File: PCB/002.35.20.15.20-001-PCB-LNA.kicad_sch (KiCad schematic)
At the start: 10 parts, among them J1 Conn_Coaxial, J2 Conn_Coaxial, J3 Conn_Coaxial, U3 YAT-1A+, U4 L7805, U5 L7805

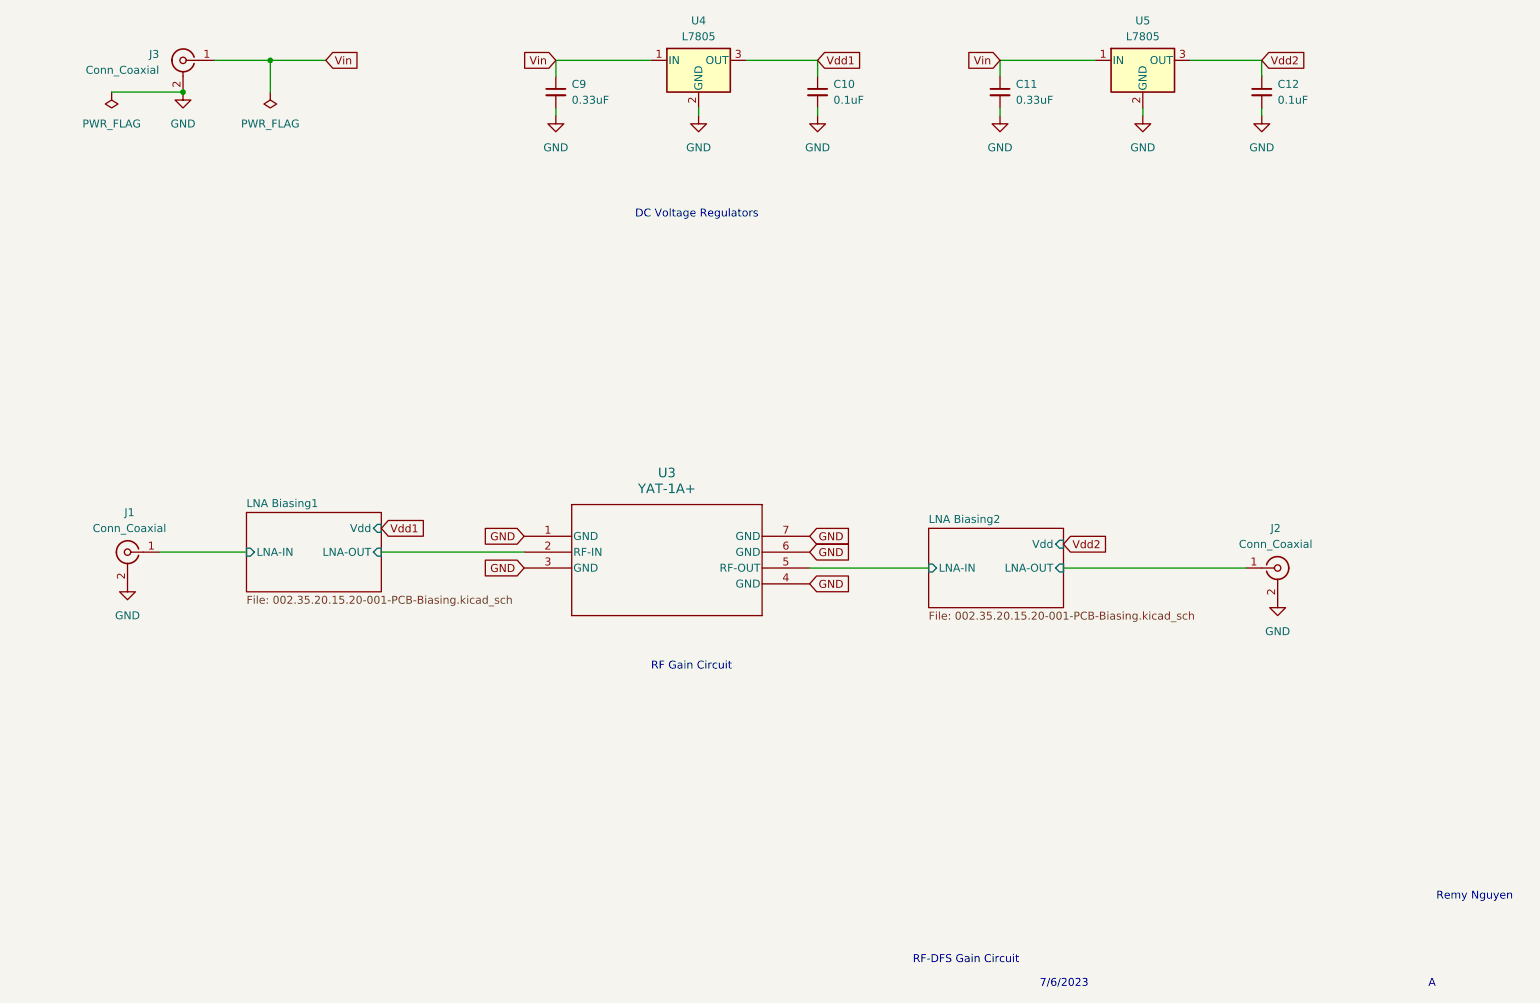
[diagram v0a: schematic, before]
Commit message: PCB Rev B complete: compacted board and fixed sma pads
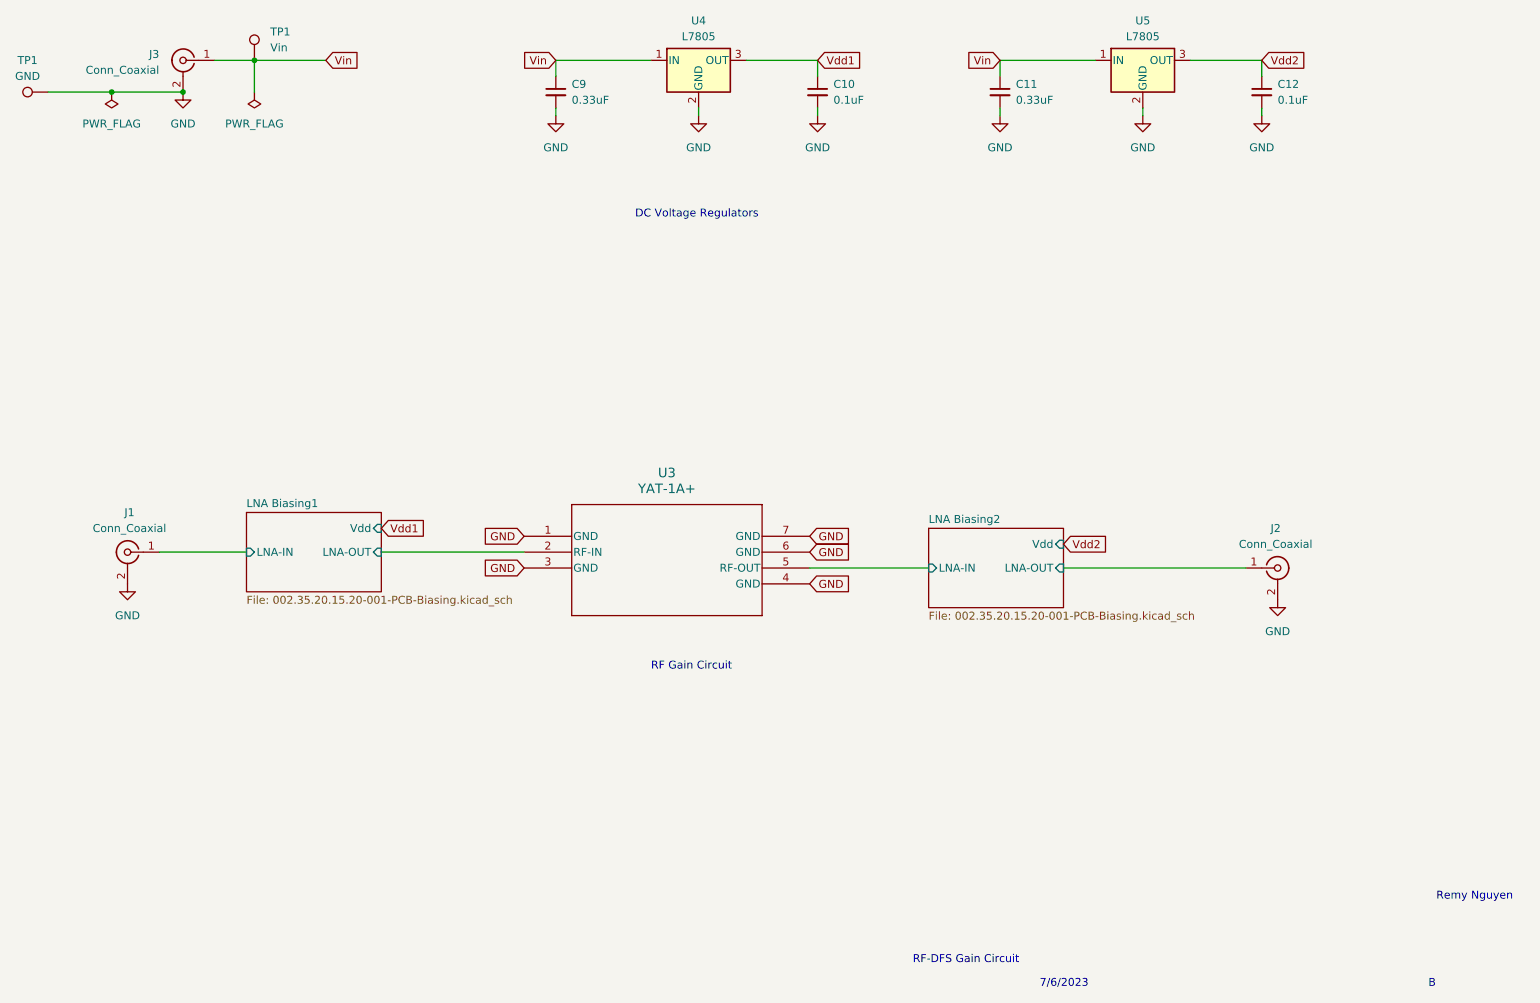
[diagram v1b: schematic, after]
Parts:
- added TP1: GND, TestPoint:TestPoint_Loop_D2.54mm_Drill1.5mm_Beaded, symbol Connector:TestPoint
- added TP1: Vin, TestPoint:TestPoint_Loop_D2.54mm_Drill1.5mm_Beaded, symbol Connector:TestPoint
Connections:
- net GND: now also TP1.1
- net Vin: now also TP1.1
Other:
- note added: "B"
- note removed: "A"
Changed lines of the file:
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@@
   (junction (at 69.85 50.8) (diameter 0) (color 0 0 0 0)
   )
-  (junction (at 83.82 45.72) (diameter 0) (color 0 0 0 0)
+  (junction (at 58.42 50.8) (diameter 0) (color 0 0 0 0)
+  )
+  (junction (at 81.28 45.72) (diameter 0) (color 0 0 0 0)
   )
   (wire (pts (xy 223.52 53.34) (xy 223.52 54.61))
@@
     (stroke (width 0) (type default))
   )
-  (wire (pts (xy 92.71 45.72) (xy 83.82 45.72))
-    (stroke (width 0) (type default))
-  )
   (wire (pts (xy 66.04 124.46) (xy 80.01 124.46))
     (stroke (width 0) (type default))
   )
-  (wire (pts (xy 83.82 45.72) (xy 74.93 45.72))
-    (stroke (width 0) (type default))
-  )
   (wire (pts (xy 129.54 48.26) (xy 129.54 45.72))
     (stroke (width 0) (type default))
@@
     (stroke (width 0) (type default))
   )
+  (wire (pts (xy 48.26 50.8) (xy 58.42 50.8))
+    (stroke (width 0) (type default))
+  )
   (wire (pts (xy 200.66 45.72) (xy 215.9 45.72))
     (stroke (width 0) (type default))
   )
+  (wire (pts (xy 81.28 45.72) (xy 92.71 45.72))
+    (stroke (width 0) (type default))
+  )
   (wire (pts (xy 210.82 127) (xy 240.03 127))
     (stroke (width 0) (type default))
   )
-  (wire (pts (xy 83.82 45.72) (xy 83.82 50.8))
+  (wire (pts (xy 81.28 45.72) (xy 81.28 50.8))
     (stroke (width 0) (type default))
   )
@@
   )
   (wire (pts (xy 242.57 53.34) (xy 242.57 54.61))
+    (stroke (width 0) (type default))
+  )
+  (wire (pts (xy 74.93 45.72) (xy 81.28 45.72))
     (stroke (width 0) (type default))
   )
@@
     (effects (font (size 1.27 1.27)) (justify left bottom))
   )
-  (text "A" (at 269.24 194.31 0)
+  (text "B" (at 269.24 194.31 0)
     (effects (font (size 1.27 1.27)) (justify left bottom))
   )
@@
     )
   )
+  (symbol (lib_id "Connector:TestPoint") (at 48.26 50.8 90) (unit 1)
+    (in_bom yes) (on_board yes) (dnp no) (fields_autoplaced)
+    (property "Reference" "TP1" (at 44.958 45.72 90)
+      (effects (font (size 1.27 1.27)))
+    )
+    (property "Value" "GND" (at 44.958 48.26 90)
+      (effects (font (size 1.27 1.27)))
+    )
+    (property "Footprint" "TestPoint:TestPoint_Loop_D2.54mm_Drill1.5mm_Beaded" (at 48.26 45.72 0)
+      (effects (font (size 1.27 1.27)) hide)
+    )
+    (property "Datasheet" "~" (at 48.26 45.72 0)
+      (effects (font (size 1.27 1.27)) hide)
+    )
+    (pin "1")
+    (instances
+      (project "002.35.20.15.20-001-PCB-LNA"
+        (path "/a33db424-96f2-4015-ba95-8b9f2330ef17/9ff85c99-1040-4eb9-b5d8-3cc01caa0e77"
+          (reference "TP1") (unit 1)
+        )
+        (path "/a33db424-96f2-4015-ba95-8b9f2330ef17/ba672304-1315-4178-9e1d-d553703e5b04"
+          (reference "TP2") (unit 1)
+        )
+        (path "/a33db424-96f2-4015-ba95-8b9f2330ef17"
+          (reference "TP4") (unit 1)
+        )
+      )
+    )
+  )
   (symbol (lib_id "power:GND") (at 152.4 54.61 0) (unit 1)
     (in_bom yes) (on_board yes) (dnp no) (fields_autoplaced)
@@
     )
   )
-  (symbol (lib_id "power:PWR_FLAG") (at 83.82 50.8 180) (unit 1)
-    (in_bom yes) (on_board yes) (dnp no) (fields_autoplaced)
-    (property "Reference" "#FLG01" (at 83.82 52.705 0)
-      (effects (font (size 1.27 1.27)) hide)
-    )
-    (property "Value" "PWR_FLAG" (at 83.82 55.88 0)
-      (effects (font (size 1.27 1.27)))
-    )
-    (property "Footprint" "" (at 83.82 50.8 0)
-      (effects (font (size 1.27 1.27)) hide)
-    )
-    (property "Datasheet" "~" (at 83.82 50.8 0)
-      (effects (font (size 1.27 1.27)) hide)
-    )
+  (symbol (lib_id "Connector:TestPoint") (at 81.28 45.72 0) (unit 1)
+    (in_bom yes) (on_board yes) (dnp no) (fields_autoplaced)
+    (property "Reference" "TP1" (at 83.82 41.148 0)
+      (effects (font (size 1.27 1.27)) (justify left))
+    )
+    (property "Value" "Vin" (at 83.82 43.688 0)
+      (effects (font (size 1.27 1.27)) (justify left))
+    )
+    (property "Footprint" "TestPoint:TestPoint_Loop_D2.54mm_Drill1.5mm_Beaded" (at 86.36 45.72 0)
+      (effects (font (size 1.27 1.27)) hide)
+    )
+    (property "Datasheet" "~" (at 86.36 45.72 0)
+      (effects (font (size 1.27 1.27)) hide)
+    )
+    (pin "1")
+    (instances
+      (project "002.35.20.15.20-001-PCB-LNA"
+        (path "/a33db424-96f2-4015-ba95-8b9f2330ef17/9ff85c99-1040-4eb9-b5d8-3cc01caa0e77"
+          (reference "TP1") (unit 1)
+        )
+        (path "/a33db424-96f2-4015-ba95-8b9f2330ef17/ba672304-1315-4178-9e1d-d553703e5b04"
+          (reference "TP2") (unit 1)
+        )
+        (path "/a33db424-96f2-4015-ba95-8b9f2330ef17"
+          (reference "TP3") (unit 1)
+        )
+      )
+    )
+  )
+  (symbol (lib_id "power:PWR_FLAG") (at 81.28 50.8 180) (unit 1)
+    (in_bom yes) (on_board yes) (dnp no) (fields_autoplaced)
+    (property "Reference" "#FLG01" (at 81.28 52.705 0)
+      (effects (font (size 1.27 1.27)) hide)
+    )
+    (property "Value" "PWR_FLAG" (at 81.28 55.88 0)
+      (effects (font (size 1.27 1.27)))
+    )
+    (property "Footprint" "" (at 81.28 50.8 0)
+      (effects (font (size 1.27 1.27)) hide)
+    )
+    (property "Datasheet" "~" (at 81.28 50.8 0)
+      (effects (font (size 1.27 1.27)) hide)
+    )

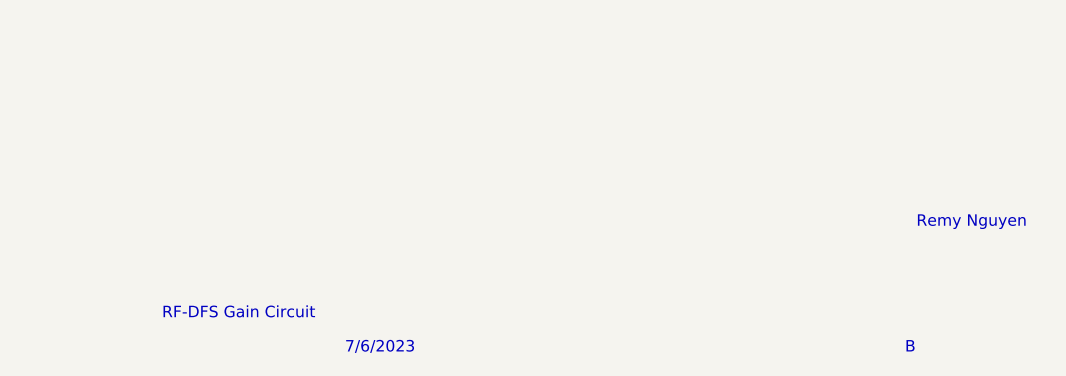
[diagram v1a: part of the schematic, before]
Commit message: Drawing sheets updated
* A4 --> Letter
* SMA connector diameter dimensioned
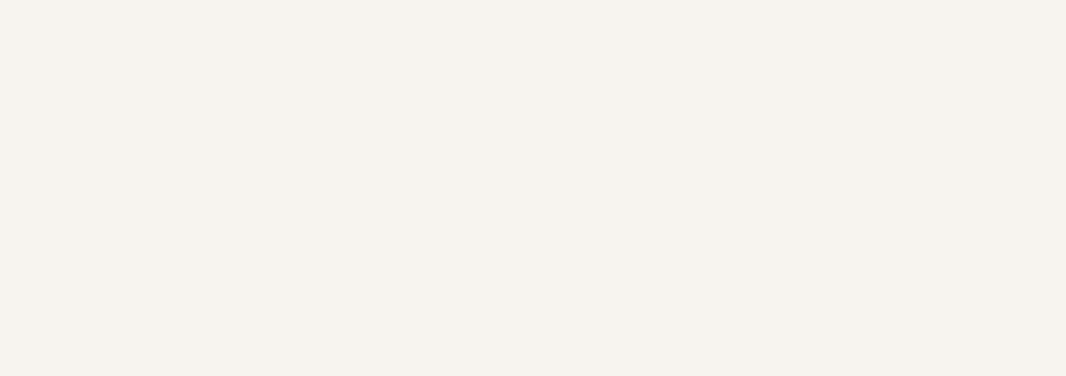
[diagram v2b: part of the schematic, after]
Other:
- note removed: "7/6/2023"
- note removed: "B"
- note removed: "RF-DFS Gain Circuit"
- note removed: "Remy Nguyen"
- company: (none) -> National Radio Astronomy Observatory
- title: (none) -> RF-DFS Gain Circuit
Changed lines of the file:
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@@
 (kicad_sch (version 20230121) (generator eeschema)
-  (paper "A4")
+  (paper "USLetter")
+  (title_block
+    (title "RF-DFS Gain Circuit")
+    (date "2/23/2024")
+    (rev "C")
+    (company "National Radio Astronomy Observatory")
+    (comment 1 "Remy Nguyen")
+  )
   (junction (at 69.85 50.8) (diameter 0) (color 0 0 0 0)
   )
@@
     (stroke (width 0) (type default))
   )
-  (text "RF-DFS Gain Circuit" (at 186.69 190.5 0)
-    (effects (font (size 1.27 1.27)) (justify left bottom))
-  )
-  (text "7/6/2023" (at 207.01 194.31 0)
-    (effects (font (size 1.27 1.27)) (justify left bottom))
-  )
-  (text "Remy Nguyen" (at 270.51 180.34 0)
-    (effects (font (size 1.27 1.27)) (justify left bottom))
-  )
-  (text "B" (at 269.24 194.31 0)
-    (effects (font (size 1.27 1.27)) (justify left bottom))
-  )
   (text "RF Gain Circuit" (at 144.78 143.51 0)
